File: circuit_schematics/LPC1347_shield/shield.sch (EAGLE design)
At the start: 17 parts, among them IC1 7805TV, IC2 LD1117V33

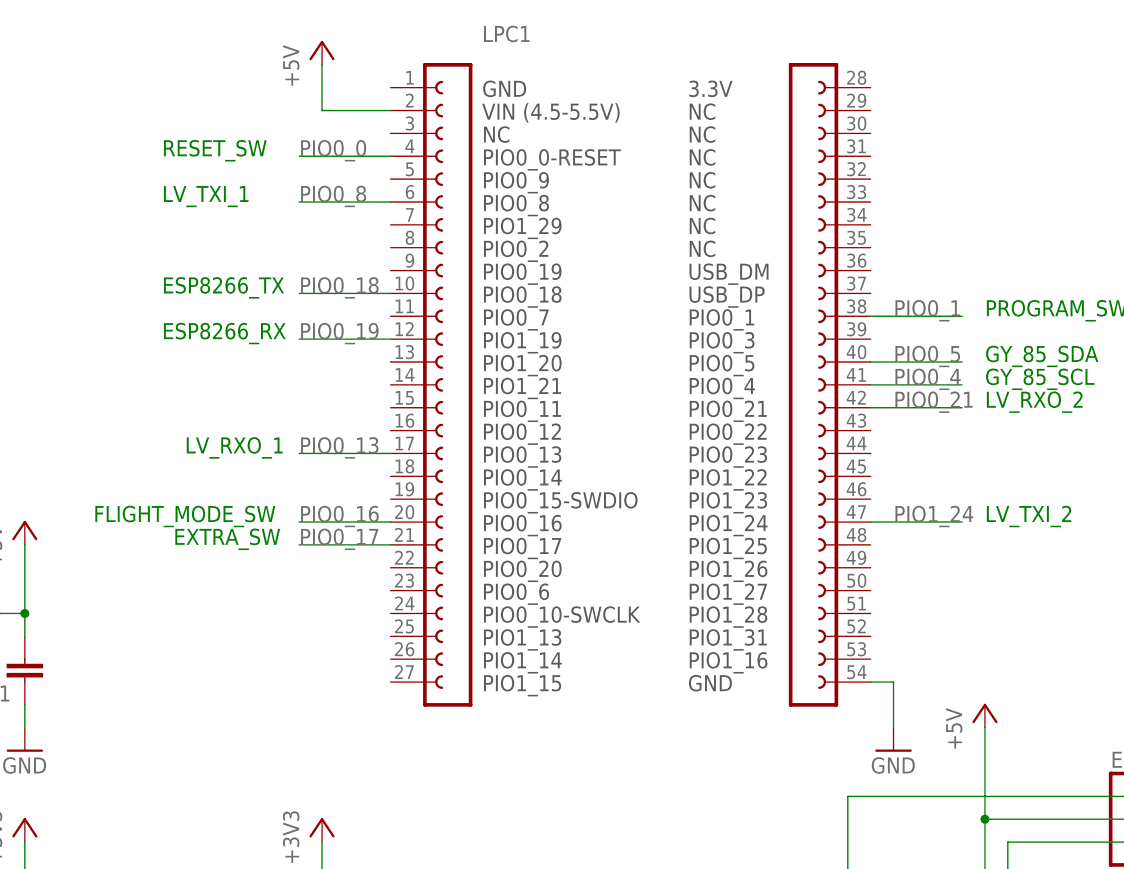
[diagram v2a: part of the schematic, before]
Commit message: Fixed Wiring Error.
Wire from ESP8266 RX must go to P0_19 not P1_19.
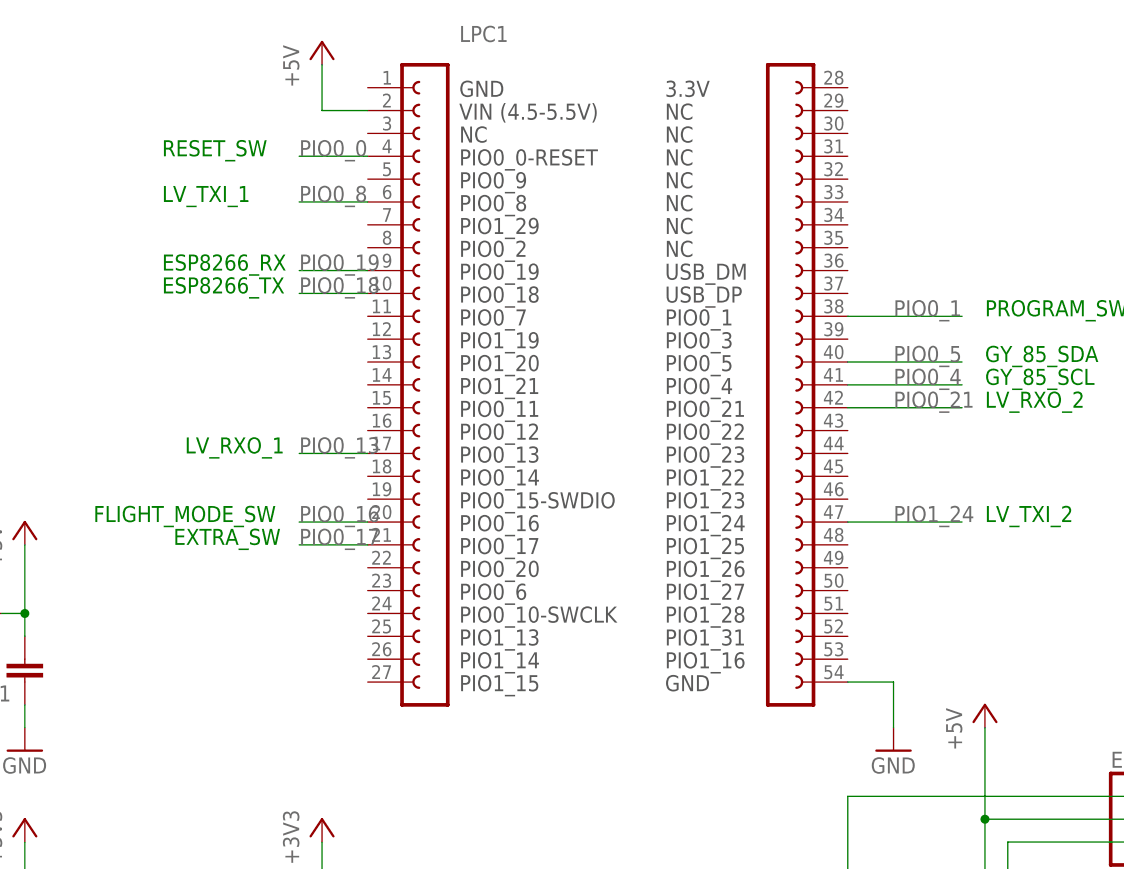
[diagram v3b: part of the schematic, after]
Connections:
- net PIO0_19: now also LPC1.9; no longer LPC1.12
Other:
- moved on the sheet: LPC1
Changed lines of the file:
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@@
 <text x="66.04" y="167.64" size="1.778" layer="91">RESET_SW</text>
 <text x="66.04" y="162.56" size="1.778" layer="91">LV_TXI_1</text>
-<text x="66.04" y="147.32" size="1.778" layer="91">ESP8266_RX</text>
 <text x="66.04" y="152.4" size="1.778" layer="91">ESP8266_TX</text>
 <text x="68.58" y="134.62" size="1.778" layer="91">LV_RXO_1</text>
@@
 <text x="157.48" y="139.7" size="1.778" layer="91">LV_RXO_2</text>
 <text x="157.48" y="127" size="1.778" layer="91">LV_TXI_2</text>
+<text x="66.04" y="154.94" size="1.778" layer="91">ESP8266_RX</text>
 </plain>
 <instances>
@@
 <instance part="P+3" gate="1" x="22.86" y="157.48"/>
 <instance part="GND5" gate="1" x="22.86" y="137.16"/>
-<instance part="LPC1" gate="G$1" x="116.84" y="142.24"/>
+<instance part="LPC1" gate="G$1" x="114.3" y="142.24"/>
 <instance part="P+4" gate="1" x="83.82" y="180.34"/>
 <instance part="GND6" gate="1" x="147.32" y="101.6"/>
@@
 <segment>
 <pinref part="LPC1" gate="G$1" pin="54"/>
-<wire x1="144.78" y1="109.22" x2="147.32" y2="109.22" width="0.1524" layer="91"/>
+<wire x1="142.24" y1="109.22" x2="147.32" y2="109.22" width="0.1524" layer="91"/>
 <pinref part="GND6" gate="1" pin="GND"/>
 <wire x1="147.32" y1="109.22" x2="147.32" y2="104.14" width="0.1524" layer="91"/>
@@
 <pinref part="LPC1" gate="G$1" pin="2"/>
 <pinref part="P+4" gate="1" pin="+5V"/>
-<wire x1="91.44" y1="172.72" x2="83.82" y2="172.72" width="0.1524" layer="91"/>
+<wire x1="88.9" y1="172.72" x2="83.82" y2="172.72" width="0.1524" layer="91"/>
 <wire x1="83.82" y1="172.72" x2="83.82" y2="177.8" width="0.1524" layer="91"/>
 </segment>
@@
 <net name="PIO0_4" class="0">
 <segment>
-<wire x1="154.94" y1="142.24" x2="144.78" y2="142.24" width="0.1524" layer="91"/>
+<wire x1="154.94" y1="142.24" x2="142.24" y2="142.24" width="0.1524" layer="91"/>
 <pinref part="LPC1" gate="G$1" pin="41"/>
 <label x="147.32" y="142.24" size="1.778" layer="95"/>
@@
 <segment>
 <pinref part="LPC1" gate="G$1" pin="4"/>
-<wire x1="91.44" y1="167.64" x2="81.28" y2="167.64" width="0.1524" layer="91"/>
+<wire x1="88.9" y1="167.64" x2="81.28" y2="167.64" width="0.1524" layer="91"/>
 <label x="81.28" y="167.64" size="1.778" layer="95"/>
 </segment>
@@
 </segment>
 <segment>
-<wire x1="154.94" y1="127" x2="144.78" y2="127" width="0.1524" layer="91"/>
+<wire x1="154.94" y1="127" x2="142.24" y2="127" width="0.1524" layer="91"/>
 <pinref part="LPC1" gate="G$1" pin="47"/>
 <label x="147.32" y="127" size="1.778" layer="95"/>
@@
 <segment>
 <pinref part="LPC1" gate="G$1" pin="6"/>
-<wire x1="91.44" y1="162.56" x2="81.28" y2="162.56" width="0.1524" layer="91"/>
+<wire x1="88.9" y1="162.56" x2="81.28" y2="162.56" width="0.1524" layer="91"/>
 <label x="81.28" y="162.56" size="1.778" layer="95"/>
 </segment>
@@
 <net name="PIO0_18" class="0">
 <segment>
-<wire x1="91.44" y1="152.4" x2="81.28" y2="152.4" width="0.1524" layer="91"/>
+<wire x1="88.9" y1="152.4" x2="81.28" y2="152.4" width="0.1524" layer="91"/>
 <pinref part="LPC1" gate="G$1" pin="10"/>
 <label x="81.28" y="152.4" size="1.778" layer="95"/>
@@
 <net name="PIO0_19" class="0">
 <segment>
-<wire x1="91.44" y1="147.32" x2="81.28" y2="147.32" width="0.1524" layer="91"/>
-<pinref part="LPC1" gate="G$1" pin="12"/>
-<label x="81.28" y="147.32" size="1.778" layer="95"/>
-</segment>
-<segment>
 <pinref part="ESP8266" gate="A" pin="1"/>
 <wire x1="208.28" y1="160.02" x2="185.42" y2="160.02" width="0.1524" layer="91"/>
 <label x="185.42" y="160.02" size="1.778" layer="95"/>
 </segment>
+<segment>
+<wire x1="88.9" y1="154.94" x2="81.28" y2="154.94" width="0.1524" layer="91"/>
+<label x="81.28" y="154.94" size="1.778" layer="95"/>
+<pinref part="LPC1" gate="G$1" pin="9"/>
+</segment>
 </net>
 <net name="PIO0_13" class="0">
 <segment>
-<wire x1="91.44" y1="134.62" x2="81.28" y2="134.62" width="0.1524" layer="91"/>
+<wire x1="88.9" y1="134.62" x2="81.28" y2="134.62" width="0.1524" layer="91"/>
 <pinref part="LPC1" gate="G$1" pin="17"/>
 <label x="81.28" y="134.62" size="1.778" layer="95"/>
@@
 <net name="PIO0_16" class="0">
 <segment>
-<wire x1="91.44" y1="127" x2="81.28" y2="127" width="0.1524" layer="91"/>
+<wire x1="88.9" y1="127" x2="81.28" y2="127" width="0.1524" layer="91"/>
 <pinref part="LPC1" gate="G$1" pin="20"/>
 <label x="81.28" y="127" size="1.778" layer="95"/>
@@
 <net name="PIO0_17" class="0">
 <segment>
-<wire x1="91.44" y1="124.46" x2="81.28" y2="124.46" width="0.1524" layer="91"/>
+<wire x1="88.9" y1="124.46" x2="81.28" y2="124.46" width="0.1524" layer="91"/>
 <pinref part="LPC1" gate="G$1" pin="21"/>
 <label x="81.28" y="124.46" size="1.778" layer="95"/>
@@
 <net name="PIO0_1" class="0">
 <segment>
-<wire x1="154.94" y1="149.86" x2="144.78" y2="149.86" width="0.1524" layer="91"/>
+<wire x1="154.94" y1="149.86" x2="142.24" y2="149.86" width="0.1524" layer="91"/>
 <pinref part="LPC1" gate="G$1" pin="38"/>
 <label x="147.32" y="149.86" size="1.778" layer="95"/>
@@
 <net name="PIO0_5" class="0">
 <segment>
-<wire x1="154.94" y1="144.78" x2="144.78" y2="144.78" width="0.1524" layer="91"/>
+<wire x1="154.94" y1="144.78" x2="142.24" y2="144.78" width="0.1524" layer="91"/>
 <pinref part="LPC1" gate="G$1" pin="40"/>
 <label x="147.32" y="144.78" size="1.778" layer="95"/>
@@
 <net name="PIO0_21" class="0">
 <segment>
-<wire x1="154.94" y1="139.7" x2="144.78" y2="139.7" width="0.1524" layer="91"/>
+<wire x1="154.94" y1="139.7" x2="142.24" y2="139.7" width="0.1524" layer="91"/>
 <pinref part="LPC1" gate="G$1" pin="42"/>
 <label x="147.32" y="139.7" size="1.778" layer="95"/>
